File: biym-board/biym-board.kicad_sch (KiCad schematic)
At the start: 1 part

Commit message: output -> servo
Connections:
- net SERVO_SIGNAL_0: now reaches FW1.20 (GPIO/6)
- net SERVO_SIGNAL_1: now reaches FW1.21 (GPIO/9)
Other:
- sheet output renamed servo
- sheet power ports: added ENABLE_BOOSTED, ENABLE_PERIPHERAL, ~{DISABLE_ALL}; removed ENABLE_BOOSTED_POWER, ENABLE_PERIPHERAL_POWER, ~{DISABLE_ALL_POWER}
- sheet servo: file output.kicad_sch -> servo.kicad_sch
- sheet servo ports: added GND, SIGNAL_0, SIGNAL_1, VDIGITAL, VSERVO; removed none

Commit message: Finished v0.1 of schematic
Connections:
- net DRIVER_PWM_A: now also FW1.23 (GPIO/11); no longer FW1.22 (GPIO/10)
- net DRIVER_PWM_B: now also FW1.24 (GPIO/12); no longer FW1.23 (GPIO/11)
- net DRIVER_PWM_C: now also FW1.25 (GPIO/13); no longer FW1.24 (GPIO/12)
- net ENABLE_PERIPHERAL_POWER: now also FW1.3 (AREF/A7/21); no longer FW1.25 (GPIO/13)
- net SERVO_SIGNAL_0: now also FW1.21 (GPIO/9); no longer FW1.20 (GPIO/6)
- net SERVO_SIGNAL_1: now also FW1.22 (GPIO/10); no longer FW1.21 (GPIO/9)
- net GPIO_0: now reaches FW1.19 (GPIO/5)
- new net GPIO_1: FW1.20 (GPIO/6)
- no-connect marks 9 -> 7
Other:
- added sheet gpio (gpio.kicad_sch)
- moved on the sheet: FW1

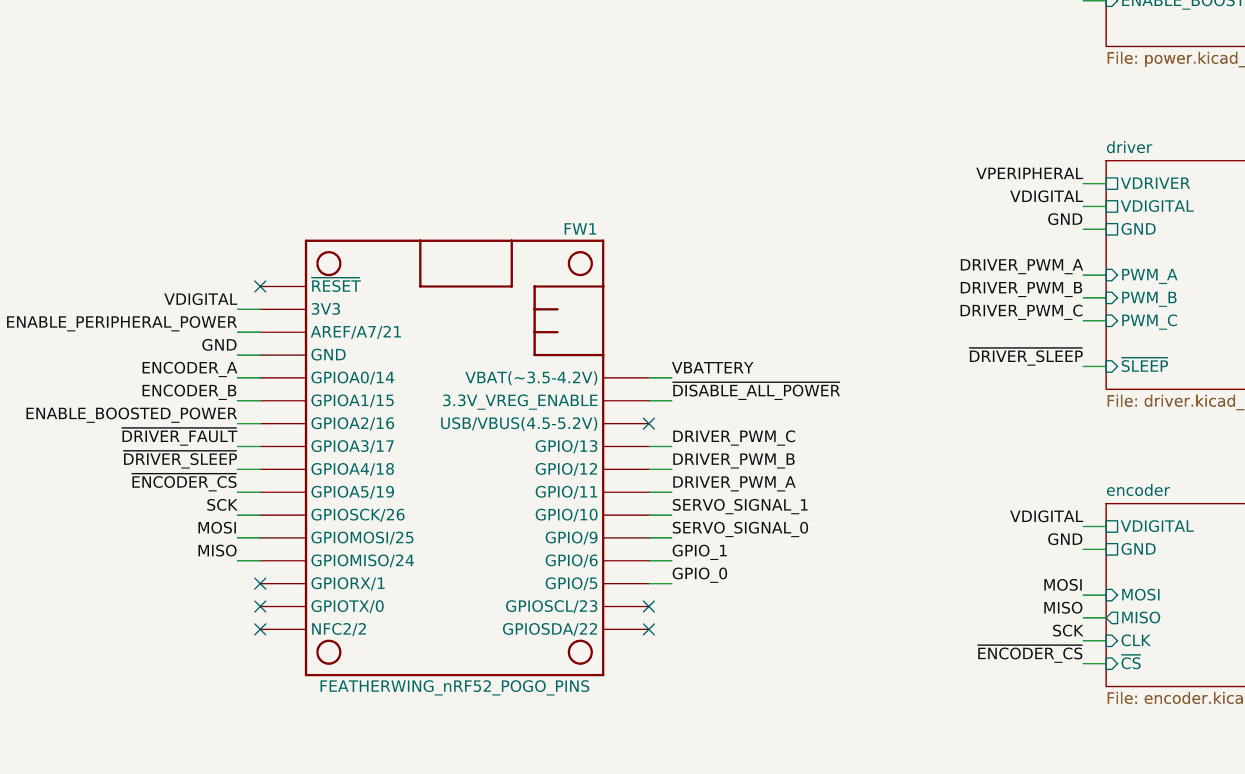
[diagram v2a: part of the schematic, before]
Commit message: Move gpio pins to rx and tx pins
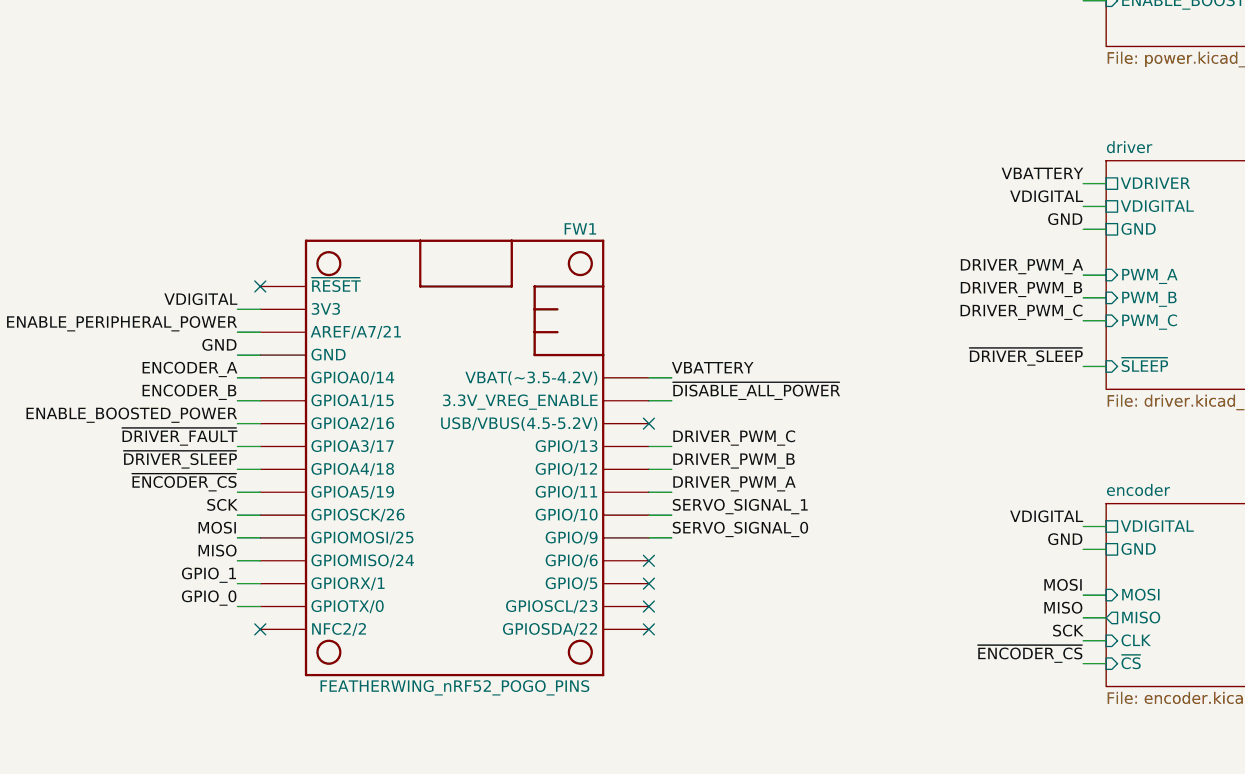
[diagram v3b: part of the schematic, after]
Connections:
- net GPIO_0: now also FW1.15 (GPIOTX/0); no longer FW1.19 (GPIO/5)
- net GPIO_1: now also FW1.14 (GPIORX/1); no longer FW1.20 (GPIO/6)
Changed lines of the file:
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@@
     (company "Peter Polidoro")
   )
-  (no_connect (at 54.61 116.84))
   (no_connect (at 97.79 119.38))
   (no_connect (at 54.61 119.38))
   (no_connect (at 54.61 81.28))
-  (no_connect (at 54.61 114.3))
   (no_connect (at 97.79 96.52))
+  (no_connect (at 97.79 114.3))
+  (no_connect (at 97.79 111.76))
   (no_connect (at 97.79 116.84))
   (wire (pts (xy 222.25 41.91) (xy 224.79 41.91))
@@
     (stroke (width 0) (type default) (color 0 0 0 0))
   )
-  (wire (pts (xy 97.79 114.3) (xy 100.33 114.3))
-    (stroke (width 0) (type default) (color 0 0 0 0))
-  )
   (wire (pts (xy 146.05 118.11) (xy 148.59 118.11))
     (stroke (width 0) (type default) (color 0 0 0 0))
@@
     (stroke (width 0) (type default) (color 0 0 0 0))
   )
+  (wire (pts (xy 54.61 116.84) (xy 52.07 116.84))
+    (stroke (width 0) (type default) (color 0 0 0 0))
+  )
   (wire (pts (xy 222.25 44.45) (xy 224.79 44.45))
     (stroke (width 0) (type default) (color 0 0 0 0))
@@
     (stroke (width 0) (type default) (color 0 0 0 0))
   )
-  (wire (pts (xy 97.79 111.76) (xy 100.33 111.76))
+  (wire (pts (xy 54.61 114.3) (xy 52.07 114.3))
     (stroke (width 0) (type default) (color 0 0 0 0))
   )
@@
     (effects (font (size 1.27 1.27)) (justify right bottom))
   )
+  (label "VBATTERY" (at 146.05 69.85 180)
+    (effects (font (size 1.27 1.27)) (justify right bottom))
+  )
   (label "GND" (at 52.07 88.9 180)
     (effects (font (size 1.27 1.27)) (justify right bottom))
@@
     (effects (font (size 1.27 1.27)) (justify right bottom))
   )
-  (label "VPERIPHERAL" (at 146.05 69.85 180)
-    (effects (font (size 1.27 1.27)) (justify right bottom))
-  )
   (label "DRIVER_PWM_A" (at 100.33 104.14 0)
     (effects (font (size 1.27 1.27)) (justify left bottom))
@@
     (effects (font (size 1.27 1.27)) (justify right bottom))
   )
+  (label "GPIO_0" (at 52.07 116.84 180)
+    (effects (font (size 1.27 1.27)) (justify right bottom))
+  )
   (label "VDIGITAL" (at 146.05 72.39 180)
     (effects (font (size 1.27 1.27)) (justify right bottom))
   )
-  (label "GPIO_1" (at 100.33 111.76 0)
-    (effects (font (size 1.27 1.27)) (justify left bottom))
+  (label "GPIO_1" (at 52.07 114.3 180)
+    (effects (font (size 1.27 1.27)) (justify right bottom))
   )
   (label "~{ENCODER_CS}" (at 146.05 123.19 180)
@@
     (effects (font (size 1.27 1.27)) (justify right bottom))
   )
-  (label "GPIO_0" (at 100.33 114.3 0)
-    (effects (font (size 1.27 1.27)) (justify left bottom))
-  )
   (label "~{ENCODER_CS}" (at 52.07 104.14 180)

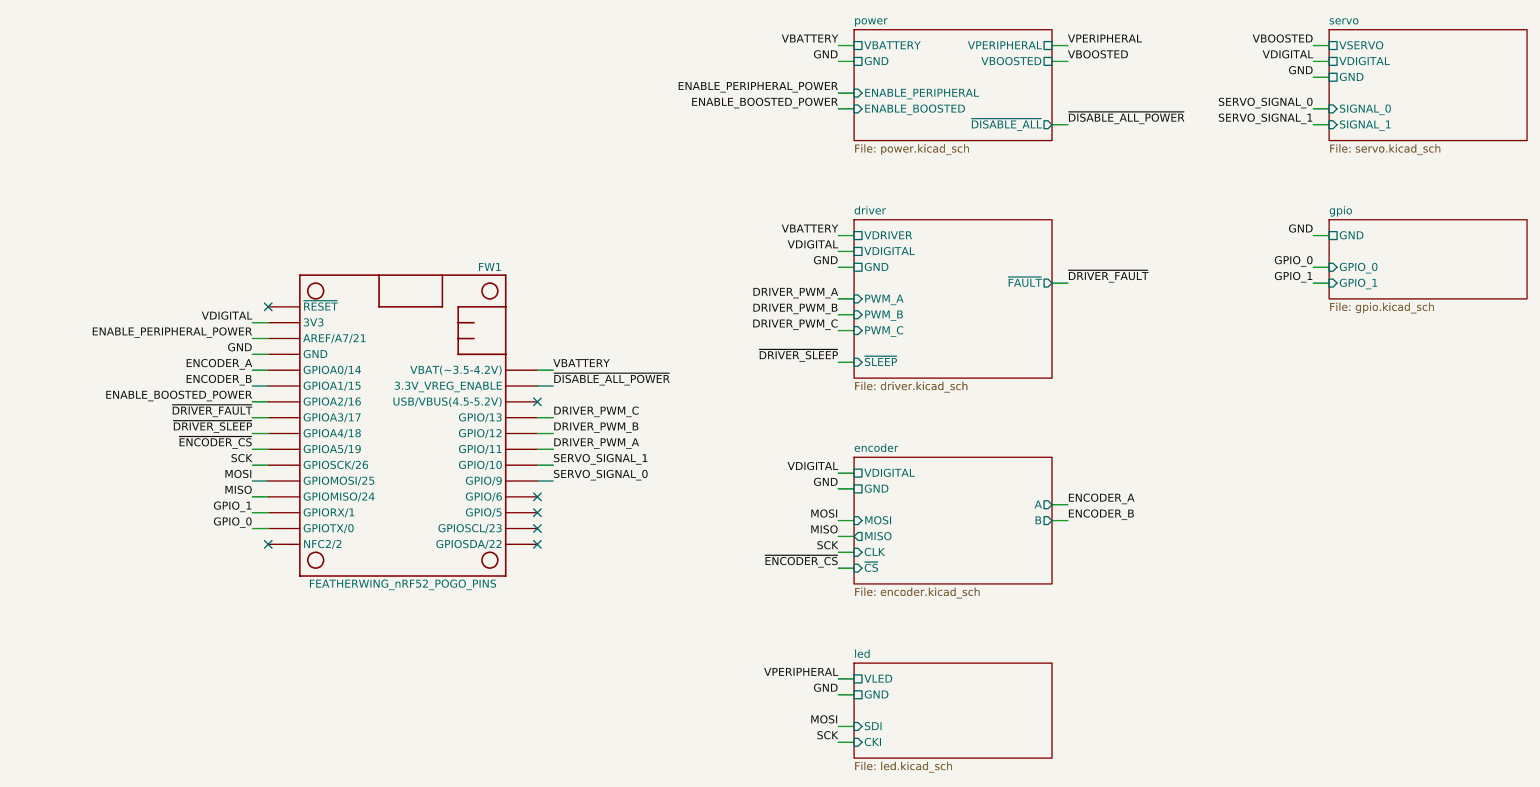
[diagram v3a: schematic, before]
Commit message: Add boost for both led and servo
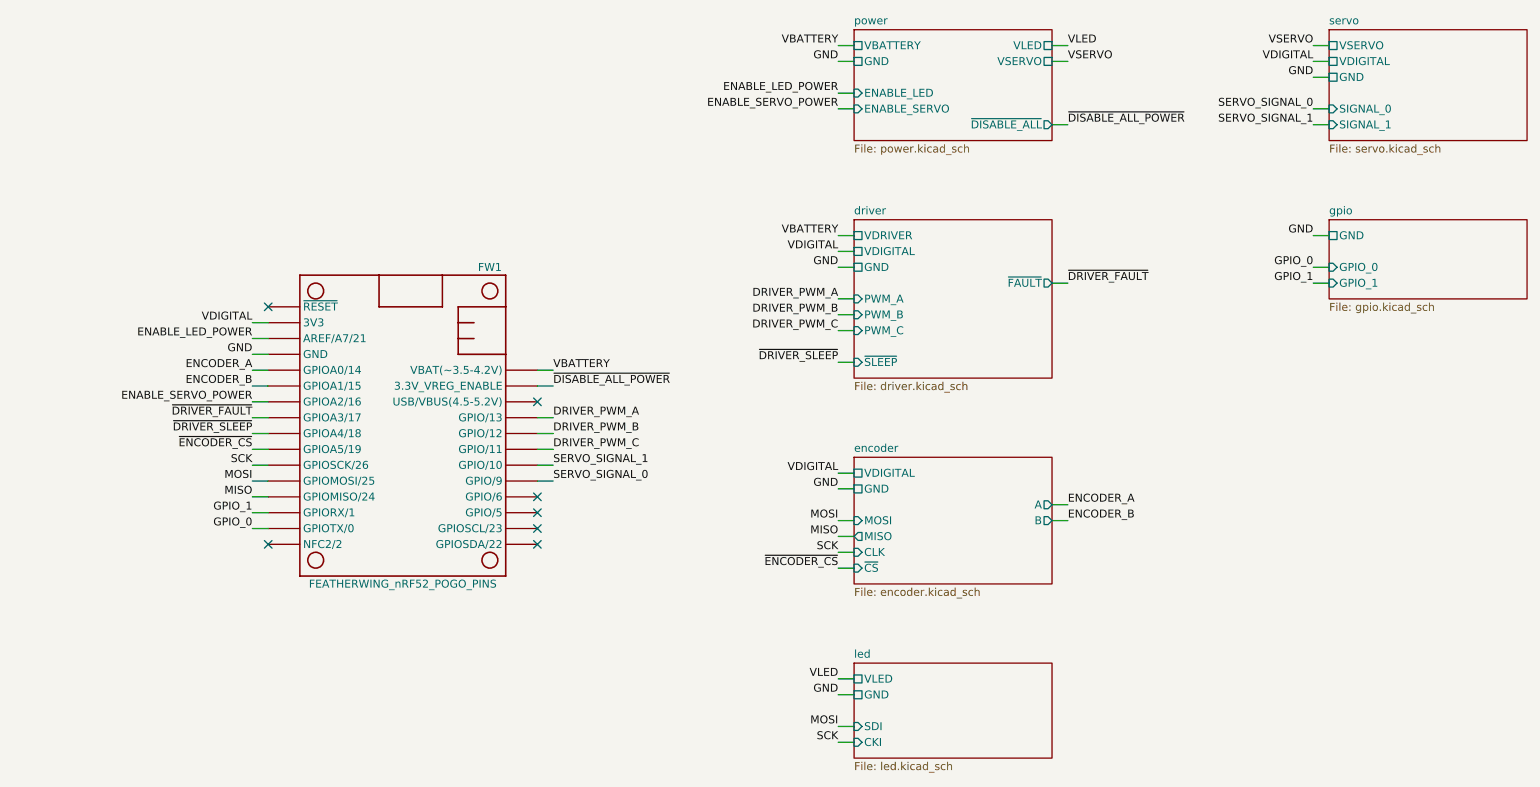
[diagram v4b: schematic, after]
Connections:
- net DRIVER_PWM_A: now also FW1.25 (GPIO/13); no longer FW1.23 (GPIO/11)
- net DRIVER_PWM_C: now also FW1.23 (GPIO/11); no longer FW1.25 (GPIO/13)
- net ENABLE_BOOSTED_POWER renamed ENABLE_SERVO_POWER
- net ENABLE_PERIPHERAL_POWER renamed ENABLE_LED_POWER
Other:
- sheet power ports: added ENABLE_LED, ENABLE_SERVO, VLED, VSERVO; removed ENABLE_BOOSTED, ENABLE_PERIPHERAL, VBOOSTED, VPERIPHERAL

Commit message: Initial footprint placement
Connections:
- net DRIVER_PWM_A: now also FW1.23 (GPIO/11); no longer FW1.25 (GPIO/13)
- net DRIVER_PWM_B: now also FW1.22 (GPIO/10); no longer FW1.24 (GPIO/12)
- net DRIVER_PWM_C: now also FW1.21 (GPIO/9); no longer FW1.23 (GPIO/11)
- net ENABLE_SERVO_POWER: now also FW1.16 (NFC2/2); no longer FW1.7 (GPIOA2/16)
- net ENCODER_A: now also FW1.20 (GPIO/6); no longer FW1.5 (GPIOA0/14)
- net ENCODER_B: now also FW1.19 (GPIO/5); no longer FW1.6 (GPIOA1/15)
- net SERVO_SIGNAL_0: now also FW1.17 (GPIOSDA/22); no longer FW1.21 (GPIO/9)
- net SERVO_SIGNAL_1: now also FW1.18 (GPIOSCL/23); no longer FW1.22 (GPIO/10)
- net ~{DRIVER_FAULT}: now also FW1.25 (GPIO/13); no longer FW1.8 (GPIOA3/17)
- net ~{DRIVER_SLEEP}: now also FW1.24 (GPIO/12); no longer FW1.9 (GPIOA4/18)

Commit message: Initial v1.0 layout
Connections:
- net ENABLE_LED_POWER: now also FW1.9 (GPIOA4/18); no longer FW1.3 (AREF/A7/21)
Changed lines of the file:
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@@
   (title_block
     (title "biym-board")
-    (date "2022-11-17")
-    (rev "0.1")
+    (date "2022-11-19")
+    (rev "1.0")
     (company "Peter Polidoro")
   )
-  (no_connect (at 54.61 101.6))
+  (no_connect (at 54.61 86.36))
   (no_connect (at 54.61 96.52))
   (no_connect (at 54.61 81.28))
@@
     (stroke (width 0) (type default) (color 0 0 0 0))
   )
-  (wire (pts (xy 54.61 86.36) (xy 52.07 86.36))
+  (wire (pts (xy 54.61 101.6) (xy 52.07 101.6))
     (stroke (width 0) (type default) (color 0 0 0 0))
   )
@@
     (effects (font (size 1.27 1.27)) (justify left bottom))
   )
-  (label "ENABLE_LED_POWER" (at 52.07 86.36 180)
+  (label "ENABLE_LED_POWER" (at 52.07 101.6 180)
     (effects (font (size 1.27 1.27)) (justify right bottom))
   )

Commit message: Completed v1.1 layout
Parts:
- removed FW1: FEATHERWING_nRF52_POGO_PINS, Janelia:FEATHERWING_POGO_PINS, symbol Janelia:FEATHERWING_nRF52_POGO_PINS
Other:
- added sheet featherwing-nrf52-pogo (featherwing-nrf52-pogo.kicad_sch)

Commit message: Finished v1.2
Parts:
- added FID1, FID2, FID3, FID4: FIDUCIAL_0.5mm_MASK1mm, Janelia:FIDUCIAL_0.5mm_Mask1mm, symbol Janelia:FIDUCIAL_0.5mm_MASK1mm
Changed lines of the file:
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@@
     (title "biym-board")
     (date "2022-11-20")
-    (rev "1.1")
+    (rev "1.2")
     (company "Peter Polidoro")
   )
@@
   (label "~{ENCODER_CS}" (at 41.91 99.06 180)
     (effects (font (size 1.27 1.27)) (justify right bottom))
+  )
+  (symbol (lib_id "Janelia:FIDUCIAL_0.5mm_MASK1mm") (at 68.58 50.8 0) (unit 1)
+    (in_bom no) (on_board yes)
+    (property "Reference" "FID3" (id 0) (at 71.12 50.8 0)
+      (effects (font (size 1.27 1.27)) (justify left))
+    )
+    (property "Value" "FIDUCIAL_0.5mm_MASK1mm" (id 1) (at 68.58 53.086 0)
+      (effects (font (size 1.27 1.27)) hide)
+    )
+    (property "Footprint" "Janelia:FIDUCIAL_0.5mm_Mask1mm" (id 2) (at 73.66 50.8 0)
+      (effects (font (size 1.27 1.27)) hide)
+    )
+    (property "Datasheet" "" (id 3) (at 73.66 50.8 0)
+      (effects (font (size 1.27 1.27)) hide)
+    )
+  )
+  (symbol (lib_id "Janelia:FIDUCIAL_0.5mm_MASK1mm") (at 68.58 55.88 0) (unit 1)
+    (in_bom no) (on_board yes)
+    (property "Reference" "FID4" (id 0) (at 71.12 55.88 0)
+      (effects (font (size 1.27 1.27)) (justify left))
+    )
+    (property "Value" "FIDUCIAL_0.5mm_MASK1mm" (id 1) (at 68.58 58.166 0)
+      (effects (font (size 1.27 1.27)) hide)
+    )
+    (property "Footprint" "Janelia:FIDUCIAL_0.5mm_Mask1mm" (id 2) (at 73.66 55.88 0)
+      (effects (font (size 1.27 1.27)) hide)
+    )
+    (property "Datasheet" "" (id 3) (at 73.66 55.88 0)
+      (effects (font (size 1.27 1.27)) hide)
+    )
+  )
+  (symbol (lib_id "Janelia:FIDUCIAL_0.5mm_MASK1mm") (at 68.58 45.72 0) (unit 1)
+    (in_bom no) (on_board yes)
+    (property "Reference" "FID2" (id 0) (at 71.12 45.72 0)
+      (effects (font (size 1.27 1.27)) (justify left))
+    )
+    (property "Value" "FIDUCIAL_0.5mm_MASK1mm" (id 1) (at 68.58 48.006 0)
+      (effects (font (size 1.27 1.27)) hide)
+    )
+    (property "Footprint" "Janelia:FIDUCIAL_0.5mm_Mask1mm" (id 2) (at 73.66 45.72 0)
+      (effects (font (size 1.27 1.27)) hide)
+    )
+    (property "Datasheet" "" (id 3) (at 73.66 45.72 0)
+      (effects (font (size 1.27 1.27)) hide)
+    )
+  )
+  (symbol (lib_id "Janelia:FIDUCIAL_0.5mm_MASK1mm") (at 68.58 40.64 0) (unit 1)
+    (in_bom no) (on_board yes)
+    (property "Reference" "FID1" (id 0) (at 71.12 40.64 0)
+      (effects (font (size 1.27 1.27)) (justify left))
+    )
+    (property "Value" "FIDUCIAL_0.5mm_MASK1mm" (id 1) (at 68.58 42.926 0)
+      (effects (font (size 1.27 1.27)) hide)
+    )
+    (property "Footprint" "Janelia:FIDUCIAL_0.5mm_Mask1mm" (id 2) (at 73.66 40.64 0)
+      (effects (font (size 1.27 1.27)) hide)
+    )
+    (property "Datasheet" "" (id 3) (at 73.66 40.64 0)
+      (effects (font (size 1.27 1.27)) hide)
+    )
   )
   (sheet (at 148.59 36.83) (size 31.75 17.78) (fields_autoplaced)
@@
       (reference "C16") (unit 1) (value "10uF") (footprint "Janelia:SM0603")
     )
+    (path "/c9c10df4-3b51-4fcf-be03-8be369b63017"
+      (reference "FID1") (unit 1) (value "FIDUCIAL_0.5mm_MASK1mm") (footprint "Janelia:FIDUCIAL_0.5mm_Mask1mm")
+    )
+    (path "/b691a290-ebc1-45f5-9920-f6d601957224"
+      (reference "FID2") (unit 1) (value "FIDUCIAL_0.5mm_MASK1mm") (footprint "Janelia:FIDUCIAL_0.5mm_Mask1mm")
+    )
+    (path "/32ccc4b0-6f97-4d28-a327-1cb837c47b11"
+      (reference "FID3") (unit 1) (value "FIDUCIAL_0.5mm_MASK1mm") (footprint "Janelia:FIDUCIAL_0.5mm_Mask1mm")
+    )
+    (path "/856017b2-ab37-48b5-8e7c-97690afc43b3"
+      (reference "FID4") (unit 1) (value "FIDUCIAL_0.5mm_MASK1mm") (footprint "Janelia:FIDUCIAL_0.5mm_Mask1mm")
+    )
     (path "/a1d9e367-d69b-4148-ac7d-1c1fa0ebb9bb/a9d03b37-2be5-4c8d-800f-d7648de4fc79"
       (reference "FW1") (unit 1) (value "FEATHERWING_nRF52") (footprint "Janelia:FEATHERWING")
@@
       (reference "L2") (unit 1) (value "2.2uH") (footprint "Janelia:INDUCTOR_VLS_HBX")
     )
-    (path "/a1d9e367-d69b-4148-ac7d-1c1fa0ebb9bb/acdc7805-9fb3-4761-9ec6-c2c291466ae7"
-      (reference "P1") (unit 1) (value "POGO_01X16_0.1IN_1_SMD") (footprint "Janelia:POGO_01x16_0.1in_SMD")
-    )
-    (path "/a1d9e367-d69b-4148-ac7d-1c1fa0ebb9bb/eaa4aaa2-449f-472d-bc0d-08b1d215904f"
-      (reference "P2") (unit 1) (value "POGO_01X12_0.1IN_1_SMD") (footprint "Janelia:POGO_01x12_0.1in_SMD")
+    (path "/a1d9e367-d69b-4148-ac7d-1c1fa0ebb9bb/7e1f8c14-a397-4d3c-9d8b-4d6788cff274"
+      (reference "P1") (unit 1) (value "POGO_01X04_0.1IN_1_SMD") (footprint "Janelia:POGO_01x04_0.1in_SMD")
+    )
+    (path "/a1d9e367-d69b-4148-ac7d-1c1fa0ebb9bb/0df15a88-88a4-4482-a181-5f2e38d647e4"
+      (reference "P2") (unit 1) (value "POGO_01X04_0.1IN_1_SMD") (footprint "Janelia:POGO_01x04_0.1in_SMD")
+    )
+    (path "/a1d9e367-d69b-4148-ac7d-1c1fa0ebb9bb/60c15f0c-f032-4887-bafe-909957879ef7"
+      (reference "P3") (unit 1) (value "POGO_01X04_0.1IN_1_SMD") (footprint "Janelia:POGO_01x04_0.1in_SMD")
+    )
+    (path "/a1d9e367-d69b-4148-ac7d-1c1fa0ebb9bb/b15e0f91-954b-43ce-94b6-7752f0db309c"
+      (reference "P4") (unit 1) (value "POGO_01X04_0.1IN_1_SMD") (footprint "Janelia:POGO_01x04_0.1in_SMD")
+    )
+    (path "/a1d9e367-d69b-4148-ac7d-1c1fa0ebb9bb/7ab950e7-9bde-40b7-b26a-ef4a48785f51"
+      (reference "P5") (unit 1) (value "POGO_01X04_0.1IN_1_SMD") (footprint "Janelia:POGO_01x04_0.1in_SMD")
+    )
+    (path "/a1d9e367-d69b-4148-ac7d-1c1fa0ebb9bb/f6a1d72d-a76c-4957-9ee8-208aaabb84a2"
+      (reference "P6") (unit 1) (value "POGO_01X04_0.1IN_1_SMD") (footprint "Janelia:POGO_01x04_0.1in_SMD")
+    )
+    (path "/a1d9e367-d69b-4148-ac7d-1c1fa0ebb9bb/59d03c2a-dfa3-4df0-bf00-1af9dc54dcf2"
+      (reference "P7") (unit 1) (value "POGO_01X04_0.1IN_1_SMD") (footprint "Janelia:POGO_01x04_0.1in_SMD")
     )
     (path "/79116d11-26fd-48fc-b8f9-7a7b774125a1/d271db0e-3caf-4df3-8d2a-fb3b0ff392cd"
